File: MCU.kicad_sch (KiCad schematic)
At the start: 39 parts, among them IC3 TCAN330DCNT, J1 SM04B-GHS-TB, J2 Conn_01x04_Pin, J3 USB_C_Receptacle_USB2.0_16P, J4 Conn_01x04_Pin, J5 Conn_01x01_Pin, SW1 SW_SPDT, U2 STM32G431CBU6, U3 ME6211C33M5, Y1 ECS-80-20-5PX-TR

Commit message: RST pin
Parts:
- added C25: 100n, Capacitor_SMD:C_0402_1005Metric, symbol Device:C_Small
- added C26: 1uF, Capacitor_SMD:C_0603_1608Metric, symbol Device:C
- added SW2: SW_Push, symbol Switch:SW_Push
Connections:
- net +3.3V: now also C26.1
- net GND: now also C25.2, C26.2, SW2.2
- net RST: now reaches U2.7 (PG10-~{RST})
- net RST: now also C25.1, SW2.1
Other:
- note added: "RST Pin"
- moved on the sheet: J4, R21, R22

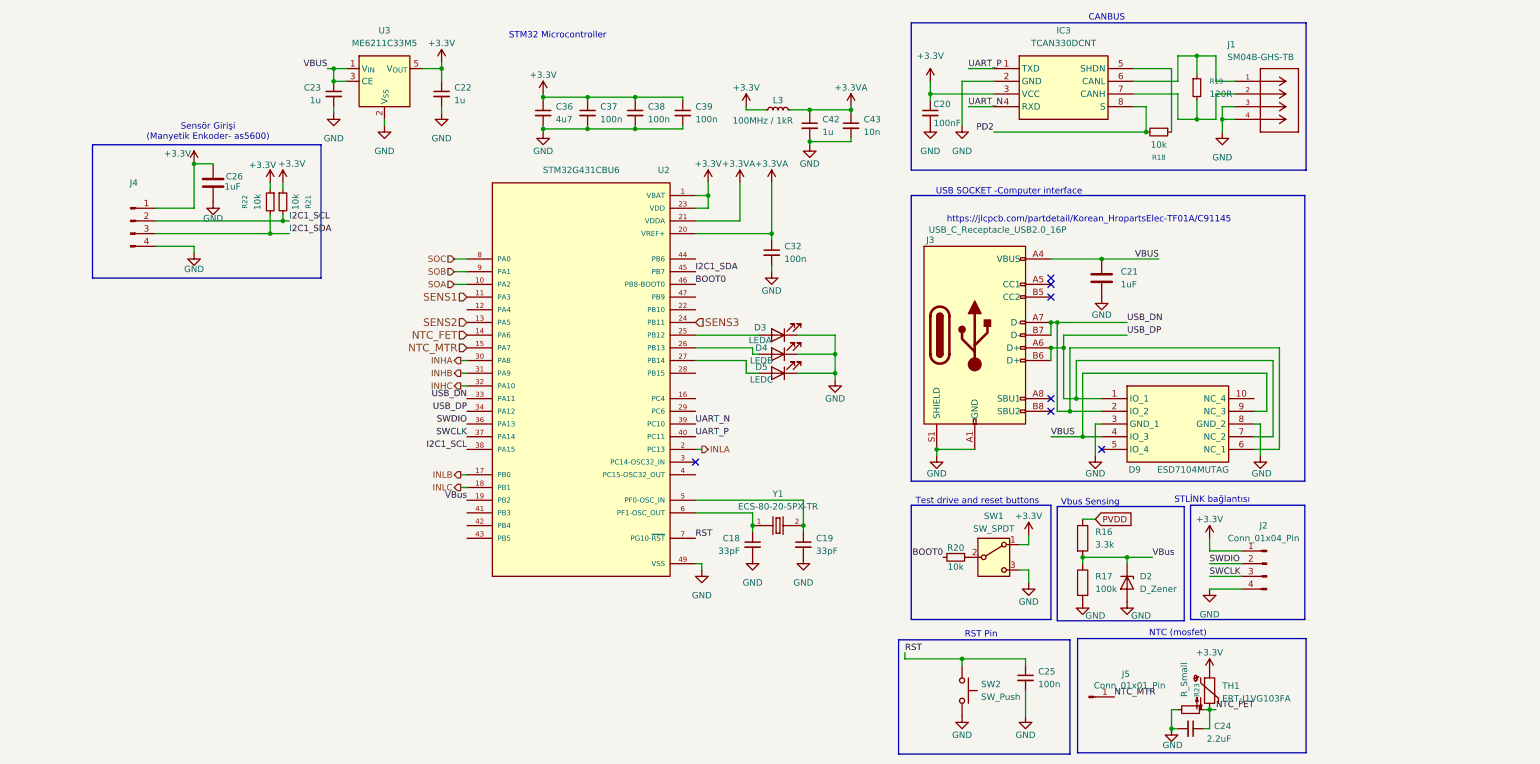
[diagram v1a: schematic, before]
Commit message: Footprints prepared, first pcb project created.
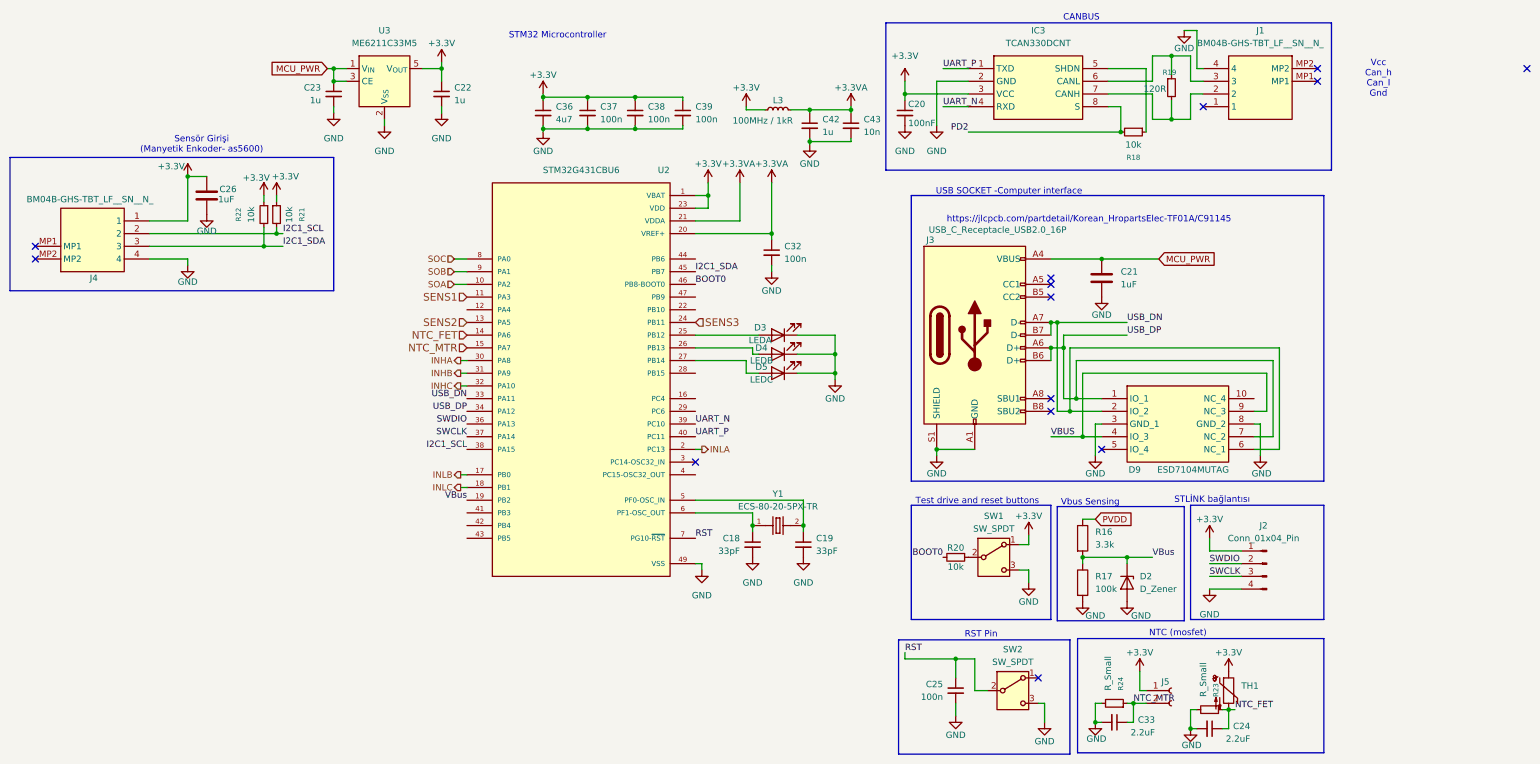
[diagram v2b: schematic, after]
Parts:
- removed J1: SM04B-GHS-TB, lib:CONN_SM04B-GHS-TB_JST, symbol lib:SM04B-GHS-TB
- removed J4: Conn_01x04_Pin, symbol Connector:Conn_01x04_Pin
- removed J5: Conn_01x01_Pin, Connector_PinHeader_1.00mm:PinHeader_1x01_P1.00mm_Vertical, symbol Connector:Conn_01x01_Pin
- removed SW2: SW_Push, symbol Switch:SW_Push
- added C33: 2.2uF, Capacitor_SMD:C_0603_1608Metric, symbol Device:C_Small
- added J1, J4: BM04B-GHS-TBT_LF__SN__N_, BM04BGHSTBTLFSNN, symbol BM04B-GHS-TBT_LF__SN__N_:BM04B-GHS-TBT_LF__SN__N_
- added J5: Conn_01x02_Socket, symbol Connector:Conn_01x02_Socket
- added R24: R_Small, Resistor_SMD:R_0603_1608Metric_Pad0.98x0.95mm_HandSolder, symbol Device:R_Small
- added SW2: SW_SPDT, Button_Switch_SMD:SW_SPDT_PCM12, symbol Switch:SW_SPDT
- D2: footprint (none) -> LIB_MMSZ4684-13P:SOD3716X135N
- D9: footprint ESD8104MUTAG -> LIB_ESD7104MUTAG:ESD8104MUTAG
- IC3: footprint lib:SOT65P280X145-8N -> LIB_TCAN330DCNT:SOT65P280X145-8N
- R16, R17: footprint (none) -> Resistor_SMD:R_0603_1608Metric_Pad0.98x0.95mm_HandSolder
- R21, R22: footprint Resistor_SMD:R_0402_1005Metric -> Resistor_SMD:R_0603_1608Metric_Pad0.98x0.95mm_HandSolder
- R23: footprint Resistor_SMD:R_0603_1608Metric -> Resistor_SMD:R_0603_1608Metric_Pad0.98x0.95mm_HandSolder
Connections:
- net +3.3V: now also J4.1, J5.1 (Pin_1)
- net GND: now also C33.2, J1.4, J4.4, R24.2, SW2.3 (C)
- net I2C1_SCL: now also J4.2
- net I2C1_SDA: now also J4.3
- net NTC_MTR: now also C33.1, J5.2 (Pin_2), R24.1
- net RST: now also SW2.2 (B)
- net VBUS: no longer C21.1, C23.1, J3.A4 (VBUS), J3.A9 (VBUS), J3.B4 (VBUS), J3.B9 (VBUS), U3.1 (V_{IN}), U3.3 (CE)
- net at IC3.6 (CANL), R19.1: now also J1.3
- net at IC3.7 (CANH), R19.2: now also J1.2
- new net MCU_PWR: C21.1, C23.1, J3.A4 (VBUS), J3.A9 (VBUS), J3.B4 (VBUS), J3.B9 (VBUS), U3.1 (V_{IN}), U3.3 (CE)
- no-connect marks 7 -> 14
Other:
- note added: "Vcc Can_h Can_l Gnd"
- moved on the sheet: C20, C24, C25, C26, IC3, R18, R19, R21, R22, R23, TH1

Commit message: component list updated, all footprints updated and now they are compatible to produce with hand (no 0402 size)
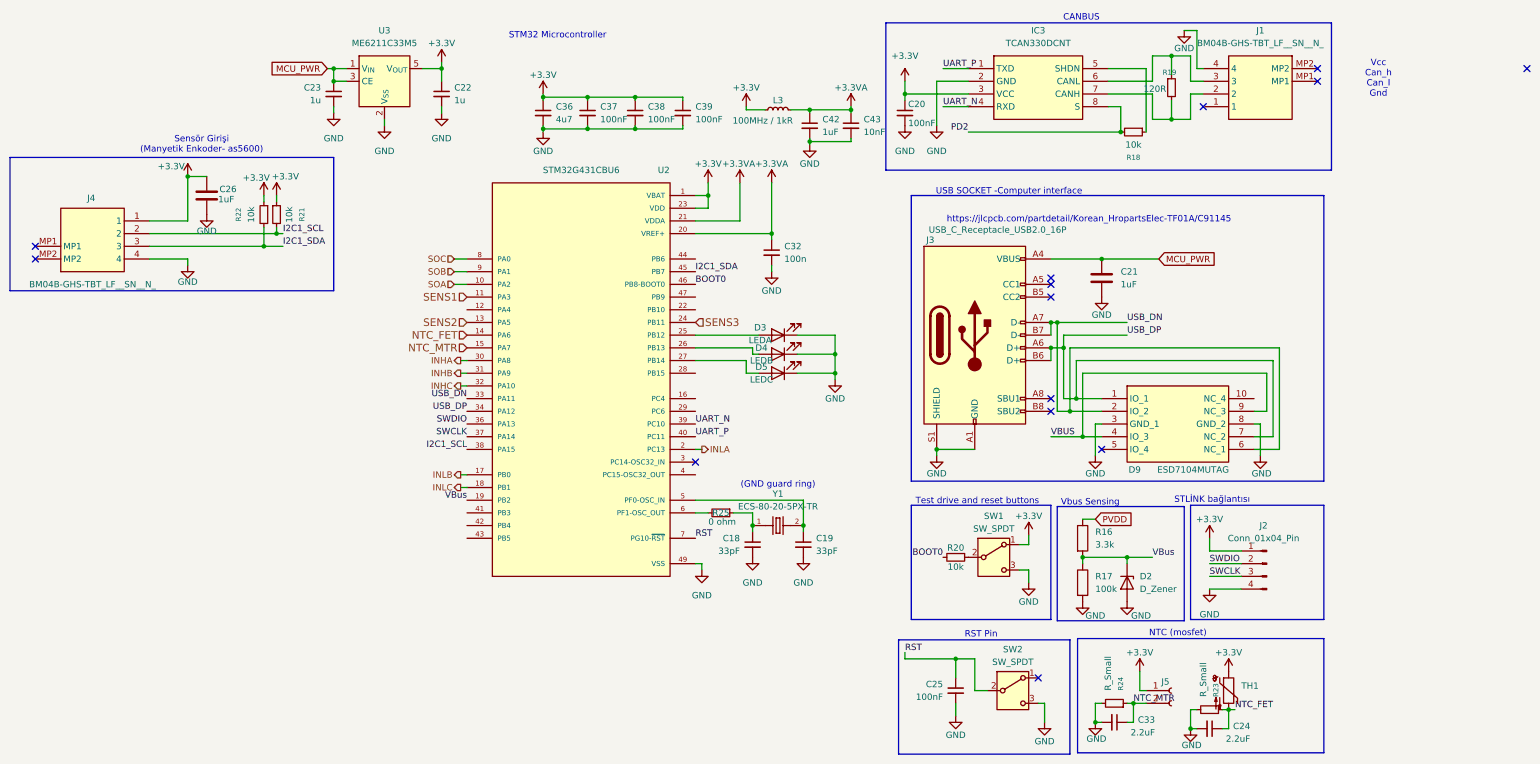
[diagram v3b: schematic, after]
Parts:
- added R25: 0 ohm, RMCF0603ZT0R00:RESC1508X55N, symbol Device:R_Small
- C18, C19: footprint (none) -> Capacitor_SMD:C_0805_2012Metric_Pad1.18x1.45mm_HandSolder
- C20, C32: footprint Capacitor_SMD:C_0402_1005Metric -> Capacitor_SMD:C_0805_2012Metric_Pad1.18x1.45mm_HandSolder
- C22, C23: footprint Capacitor_SMD:C_0402_1005Metric -> Capacitor_SMD:C_0603_1608Metric_Pad1.08x0.95mm_HandSolder
- C25, C37, C38, C39: value 100n -> 100nF; footprint Capacitor_SMD:C_0402_1005Metric -> Capacitor_SMD:C_0805_2012Metric_Pad1.18x1.45mm_HandSolder
- C42: value 1u -> 1uF; footprint Capacitor_SMD:C_0402_1005Metric -> Capacitor_SMD:C_0603_1608Metric_Pad1.08x0.95mm_HandSolder
- C43: value 10n -> 10nF; footprint Capacitor_SMD:C_0402_1005Metric -> Capacitor_SMD:C_0603_1608Metric_Pad1.08x0.95mm_HandSolder
- J1, J4: footprint BM04BGHSTBTLFSNN -> ul_BM04B-GHS-TBT-LF-SN-N-:JST_BM04B-GHS-TBT_LF__SN__N_
- J5: footprint (none) -> TerminalBlock:TerminalBlock_MaiXu_MX126-5.0-02P_1x02_P5.00mm
- R18, R19, R20: footprint Resistor_SMD:R_0402_1005Metric -> Resistor_SMD:R_0603_1608Metric_Pad0.98x0.95mm_HandSolder
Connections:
- net at C18.1, Y1.1: now also R25.1; no longer U2.6 (PF1-OSC_OUT)
- new net: R25.2, U2.6 (PF1-OSC_OUT)
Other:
- note added: "(GND guard ring)"

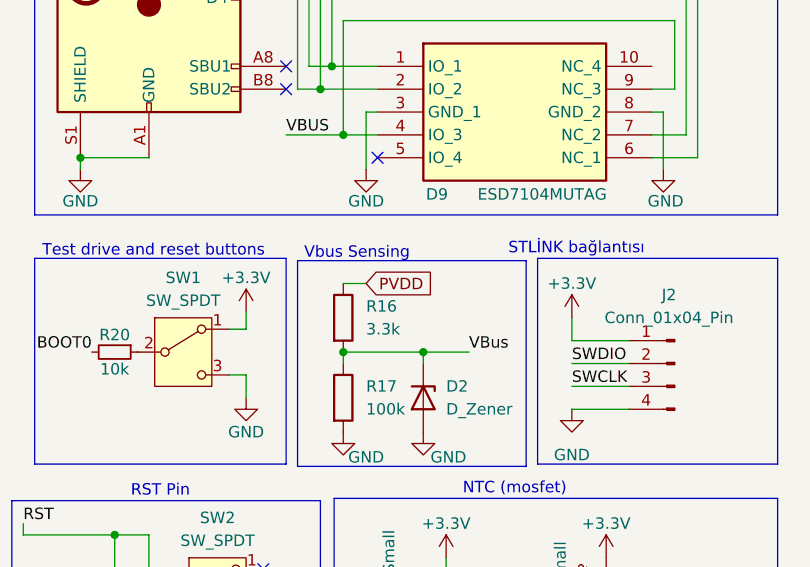
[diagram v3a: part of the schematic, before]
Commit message: some tags chaneged, pcb thinked about pcb component placement, aluminum mosfet carrier pcb and paralelling mosfets
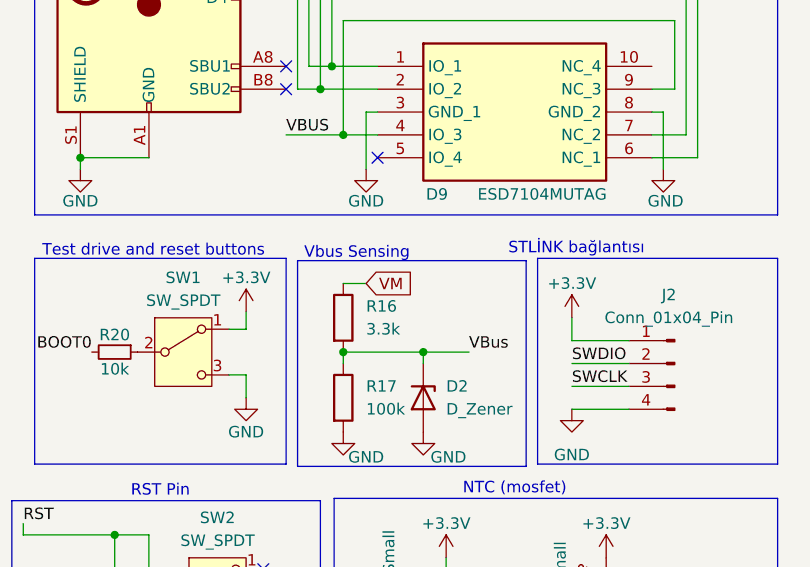
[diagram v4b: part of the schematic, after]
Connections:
- net PVDD renamed VM
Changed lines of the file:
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@@
 		)
 	)
-	(global_label "PVDD"
+	(global_label "VM"
 		(shape input)
 		(at 234.95 119.38 0)

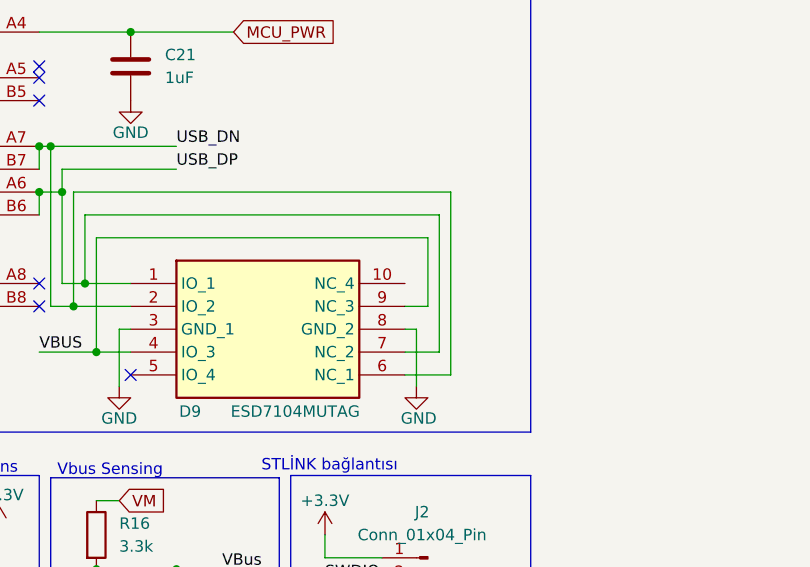
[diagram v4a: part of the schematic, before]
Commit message: starting with pcb (kicad_pcb 	(version 20241229) 	(generator "pcbnew") 	(generator_version "9.0") 	(layers 		(0 "F.Cu" signal) 		(2 "B.Cu" signal) 		(9 "F.Adhes" user "F.Adhesive") 		(11 "B.Adhes" user "B.Adhesive") 		(13 "F.Paste" user) 		(15 "B.Paste" user) 		(5 "F.SilkS" user "F.Silkscreen") 		(7 "B.SilkS" user "B.Silkscreen") 		(1 "F.Mask" user) 		(3 "B.Mask" user) 		(17 "Dwgs.User" user "User.Drawings") 		(19 "Cmts.User" user "User.Comments") 		(21 "Eco1.User" user "User.Eco1") 		(23 "Eco2.User" user "User.Eco2") 		(25 "Edge.Cuts" user) 		(27 "Margin" user) 		(31 "F.CrtYd" user "F.Courtyard") 		(29 "B.CrtYd" user "B.Courtyard") 		(35 "F.Fab" user) 		(33 "B.Fab" user) 		(39 "User.1" user) 		(41 "User.2" user) 		(43 "User.3" user) 		(45 "User.4" user) 	) 	(net 0 "") 	(net 1 "Net-(U1-CPH)") 	(net 2 "Net-(U1-CPL)") 	(net 3 "/Gate_Driver/DVDD") 	(net 4 "GND") 	(net 5 "/Gate_Driver/AGND") 	(net 6 "Net-(U1-VCP)") 	(net 7 "Net-(D1-K)") 	(net 8 "Net-(U1-CB)") 	(net 9 "MCU_PWR") 	(net 10 "/Gate_Driver/SENS1") 	(net 11 "/Gate_Driver/SENS2") 	(net 12 "/Gate_Driver/SENS3") 	(net 13 "+3.3V") 	(net 14 "/MCU/NTC_FET") 	(net 15 "/MCU/RST") 	(net 16 "+3.3VA") 	(net 17 "/MCU/NTC_MTR") 	(net 18 "/MCU/VBus") 	(net 19 "Net-(D3-A)") 	(net 20 "Net-(D4-A)") 	(net 21 "Net-(D5-A)") 	(net 22 "unconnected-(D9-IO_4-Pad5)") 	(net 23 "/MCU/USB_DP") 	(net 24 "/MCU/USB_DN") 	(net 25 "/MCU/VBUS") 	(net 26 "unconnected-(D9-NC_4-Pad10)") 	(net 27 "/MCU/UART_P") 	(net 28 "/MCU/UART_N") 	(net 29 "Net-(IC3-CANH)") 	(net 30 "/MCU/PD2") 	(net 31 "Net-(IC3-CANL)") 	(net 32 "Net-(IC3-SHDN)") 	(net 33 "unconnected-(J1-Pad1)") 	(net 34 "Net-(C18-Pad1)") 	(net 35 "/MCU/SWDIO") 	(net 36 "/MCU/SWCLK") 	(net 37 "unconnected-(J3-CC2-PadB5)") 	(net 38 "unconnected-(J3-CC1-PadA5)") 	(net 39 "unconnected-(J3-SBU1-PadA8)") 	(net 40 "unconnected-(J3-SBU2-PadB8)") 	(net 41 "/MCU/I2C1_SDA") 	(net 42 "/MCU/I2C1_SCL") 	(net 43 "/Gate_Driver/SHA") 	(net 44 "Net-(Q7-G)") 	(net 45 "/Gate_Driver/SPA") 	(net 46 "Net-(Q8-G)")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
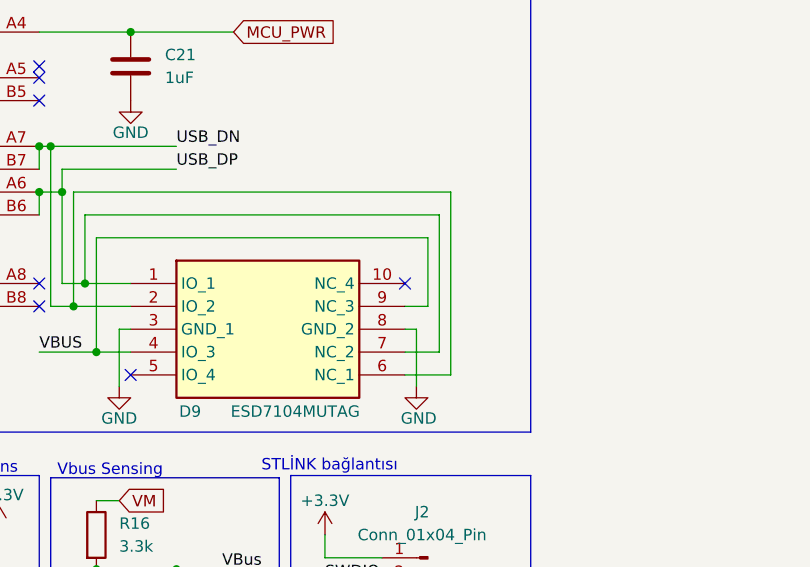
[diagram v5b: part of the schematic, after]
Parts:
- C20, C32, C37, C38, C39: footprint Capacitor_SMD:C_0805_2012Metric_Pad1.18x1.45mm_HandSolder -> Capacitor_SMD:C_0603_1608Metric_Pad1.08x0.95mm_HandSolder
- C36: footprint Capacitor_SMD:C_0603_1608Metric -> Capacitor_SMD:C_0603_1608Metric_Pad1.08x0.95mm_HandSolder
- L3: footprint Inductor_SMD:L_0402_1005Metric -> Inductor_SMD:L_0603_1608Metric_Pad1.05x0.95mm_HandSolder
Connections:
- no-connect marks 14 -> 15
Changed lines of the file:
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@@
 	)
 	(no_connect
+		(at 266.7 95.25)
+	)
+	(no_connect
 		(at 154.94 107.95)
 	)
@@
 			)
 		)
-		(property "Footprint" "Inductor_SMD:L_0402_1005Metric"
+		(property "Footprint" "Inductor_SMD:L_0603_1608Metric_Pad1.05x0.95mm_HandSolder"
 			(at 171.45 37.465 0)
 			(effects
@@
 			)
 		)
-		(property "Footprint" "Capacitor_SMD:C_0805_2012Metric_Pad1.18x1.45mm_HandSolder"
+		(property "Footprint" "Capacitor_SMD:C_0603_1608Metric_Pad1.08x0.95mm_HandSolder"
 			(at 152.4 38.1 0)
 			(effects
@@
 			)
 		)
-		(property "Footprint" "Capacitor_SMD:C_0805_2012Metric_Pad1.18x1.45mm_HandSolder"
+		(property "Footprint" "Capacitor_SMD:C_0603_1608Metric_Pad1.08x0.95mm_HandSolder"
 			(at 196.85 38.1 0)
 			(effects
@@
 			)
 		)
-		(property "Footprint" "Capacitor_SMD:C_0805_2012Metric_Pad1.18x1.45mm_HandSolder"
+		(property "Footprint" "Capacitor_SMD:C_0603_1608Metric_Pad1.08x0.95mm_HandSolder"
 			(at 170.18 66.04 0)
 			(effects
@@
 			)
 		)
-		(property "Footprint" "Capacitor_SMD:C_0805_2012Metric_Pad1.18x1.45mm_HandSolder"
+		(property "Footprint" "Capacitor_SMD:C_0603_1608Metric_Pad1.08x0.95mm_HandSolder"
 			(at 142.875 38.1 0)
 			(effects
@@
 			)
 		)
-		(property "Footprint" "Capacitor_SMD:C_0805_2012Metric_Pad1.18x1.45mm_HandSolder"
+		(property "Footprint" "Capacitor_SMD:C_0603_1608Metric_Pad1.08x0.95mm_HandSolder"
 			(at 133.35 38.1 0)
 			(effects
@@
 			)
 		)
-		(property "Footprint" "Capacitor_SMD:C_0603_1608Metric"
+		(property "Footprint" "Capacitor_SMD:C_0603_1608Metric_Pad1.08x0.95mm_HandSolder"
 			(at 124.46 38.1 0)
 			(effects
